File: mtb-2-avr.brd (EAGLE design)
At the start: 27 x 22 mm, 18 parts, among them IC1 MEGA8A-AU, Q1/2 14.745 MHz, Q2 14.745 MHz

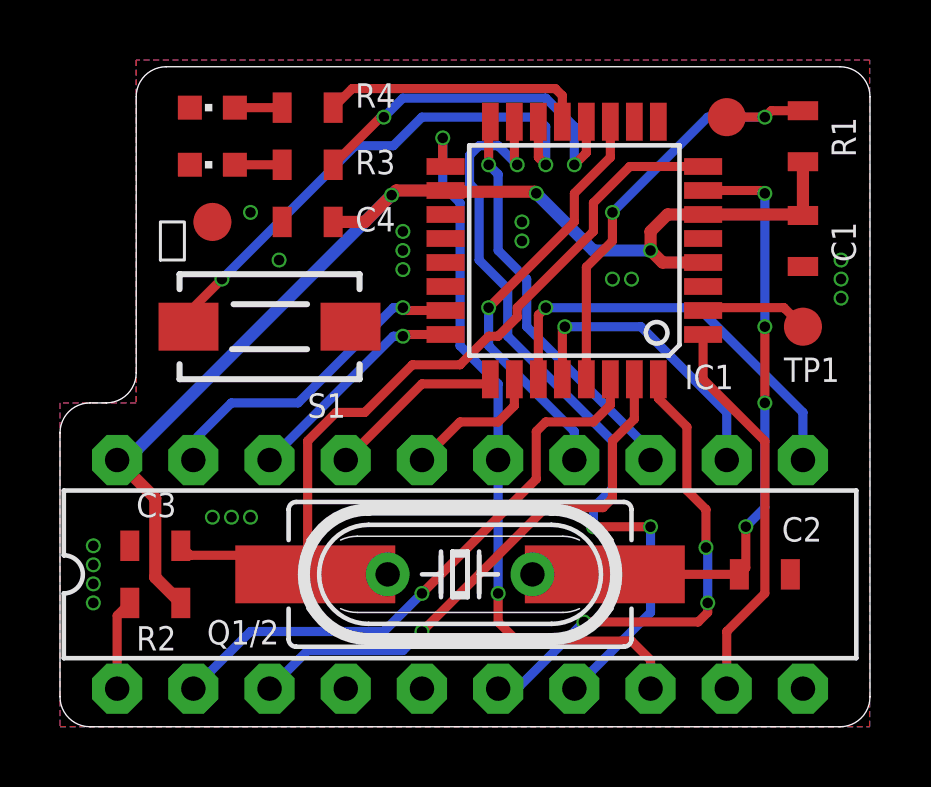
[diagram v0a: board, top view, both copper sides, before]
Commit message: Free PB2, connect SHIFT_OE.
PB2 must be free because SPI uses it. Disconnected SHIFT_OE was bug.
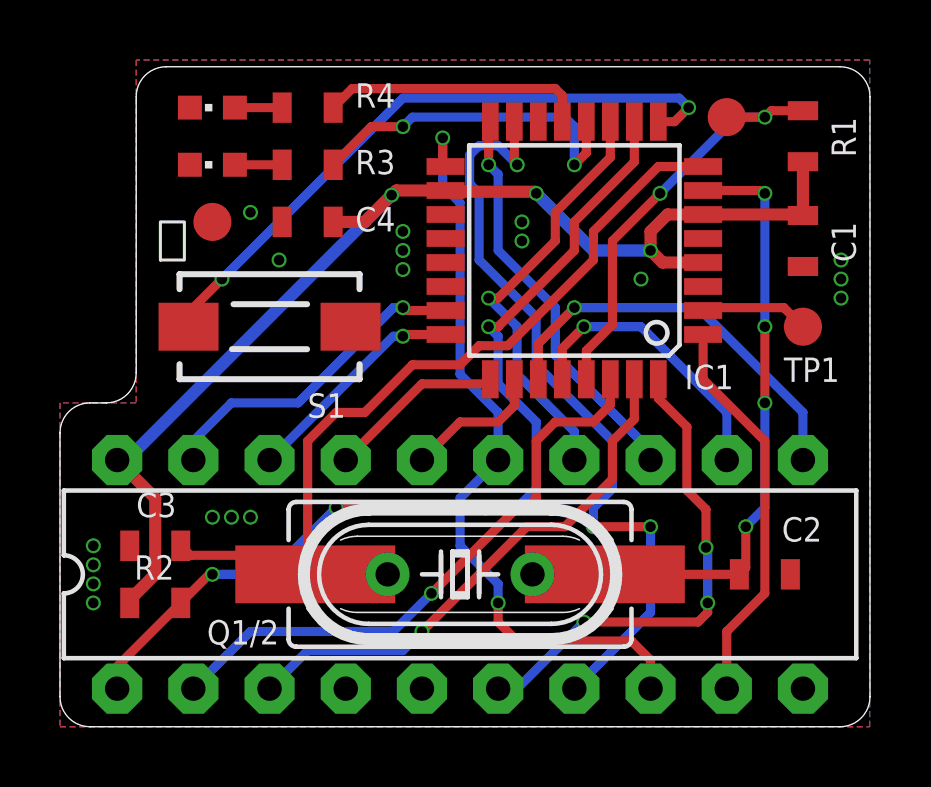
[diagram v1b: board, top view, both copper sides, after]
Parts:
- turned R2 to 180 degrees
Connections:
- removed net N$5: IC1.14, S1.2
- new net BTN: IC1.9, S1.2
- net !SHIFT_OE: now also IC1.10
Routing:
- net !SHIFT_OE: track 3.03 -> 32.2 mm, vias 0 -> 4
- net BTN: track 0.00 -> 21.4 mm, vias 0 -> 2
- net N$5: track 18.0 -> 0.00 mm, vias 2 -> 0
- net SCK: track 24.5 -> 25.5 mm
- net SDA: track 14.1 -> 13.5 mm
- net RESET: track 14.9 -> 14.4 mm
- net LED_GREEN: track 12.2 -> 11.7 mm
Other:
- board text added: "v1.1 JH 2021"
- board text removed: "v1.0 JH 2021"

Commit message: CPU socket: drills 0.8 mm → 1.0 mm
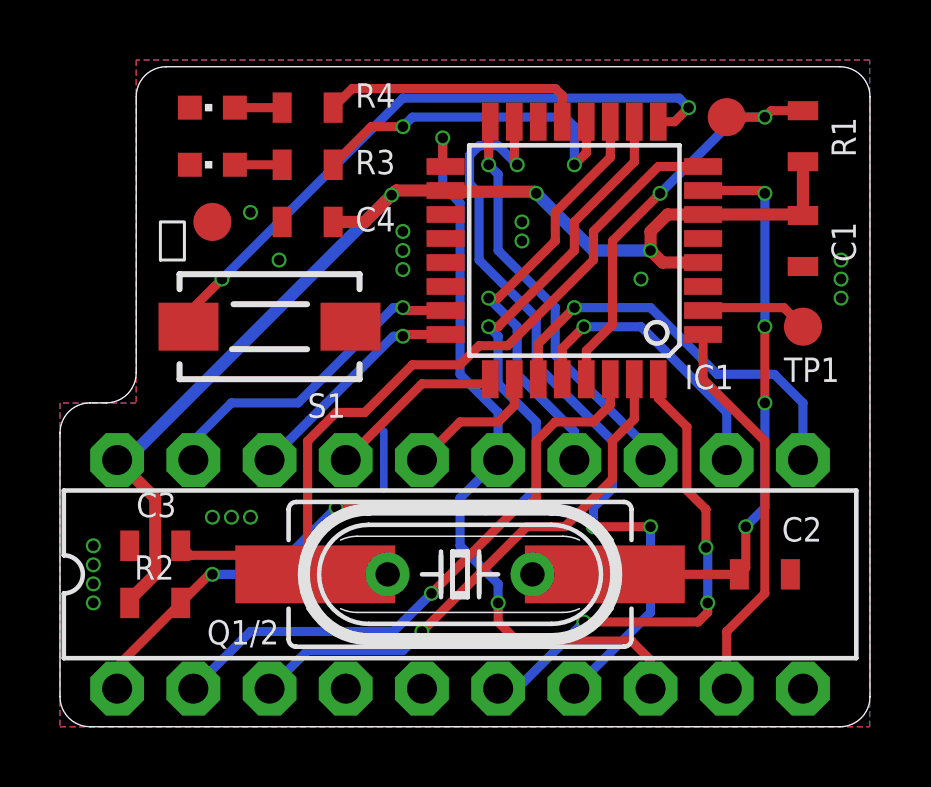
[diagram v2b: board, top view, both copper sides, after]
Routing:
- net GND: track 0.00 -> 1.90 mm
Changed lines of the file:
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@@
 <via x="6.35" y="17.145" extent="1-16" drill="0.35"/>
 <via x="7.3025" y="15.5575" extent="1-16" drill="0.35"/>
+<wire x1="10.795" y1="7.9375" x2="10.795" y2="9.8425" width="0.254" layer="16"/>
 </signal>
 <signal name="VCC">
@@
 <contactref element="TORIG" pad="11"/>
 <contactref element="IC1" pad="27"/>
-<wire x1="24.765" y1="8.89" x2="24.765" y2="10.4775" width="0.3048" layer="16"/>
-<wire x1="24.765" y1="10.4775" x2="21.2725" y2="13.97" width="0.3048" layer="16"/>
-<wire x1="21.2725" y1="13.97" x2="17.145" y2="13.97" width="0.3048" layer="16"/>
+<wire x1="24.765" y1="8.89" x2="24.765" y2="10.795" width="0.3048" layer="16"/>
+<wire x1="24.765" y1="10.795" x2="23.8125" y2="11.7475" width="0.3048" layer="16"/>
+<wire x1="23.8125" y1="11.7475" x2="21.9075" y2="11.7475" width="0.3048" layer="16"/>
+<wire x1="21.9075" y1="11.7475" x2="19.685" y2="13.97" width="0.3048" layer="16"/>
+<wire x1="19.685" y1="13.97" x2="17.145" y2="13.97" width="0.3048" layer="16"/>
 <wire x1="15.945" y1="11.5824" x2="15.945" y2="12.77" width="0.3048" layer="1"/>
 <wire x1="15.945" y1="12.77" x2="17.145" y2="13.97" width="0.3048" layer="1"/>
